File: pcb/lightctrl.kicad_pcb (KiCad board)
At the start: 2 copper layers, 76.8 x 36.8 mm, 30 parts, among them IC1 ESP-WROOM-02, P1 LED_CONN, P2 PROG, P3 IO, P4 BATT_SENSE, P5 5V, Q1 BSS138, Q2 IRF8788, SW1 SW_FLASH, SW2 SW_RST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

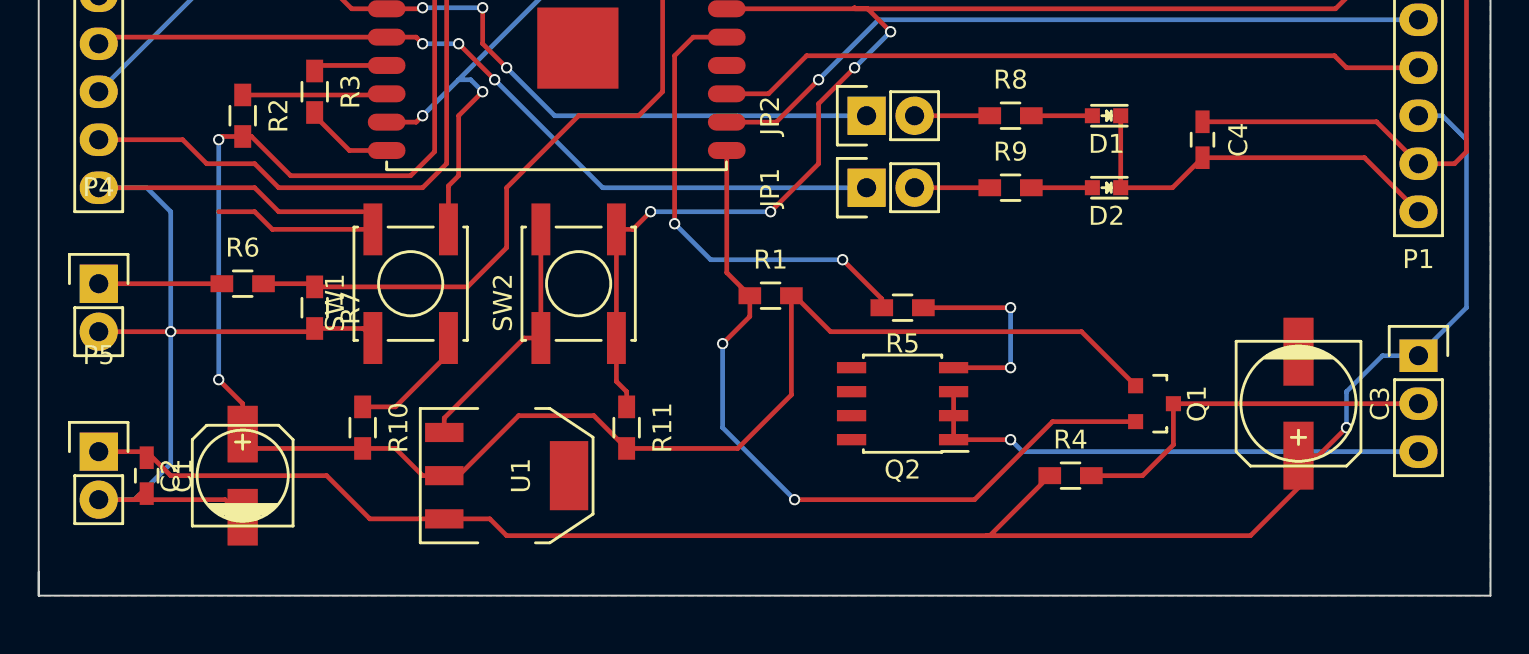
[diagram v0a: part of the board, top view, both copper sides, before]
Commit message: Thicker power traces
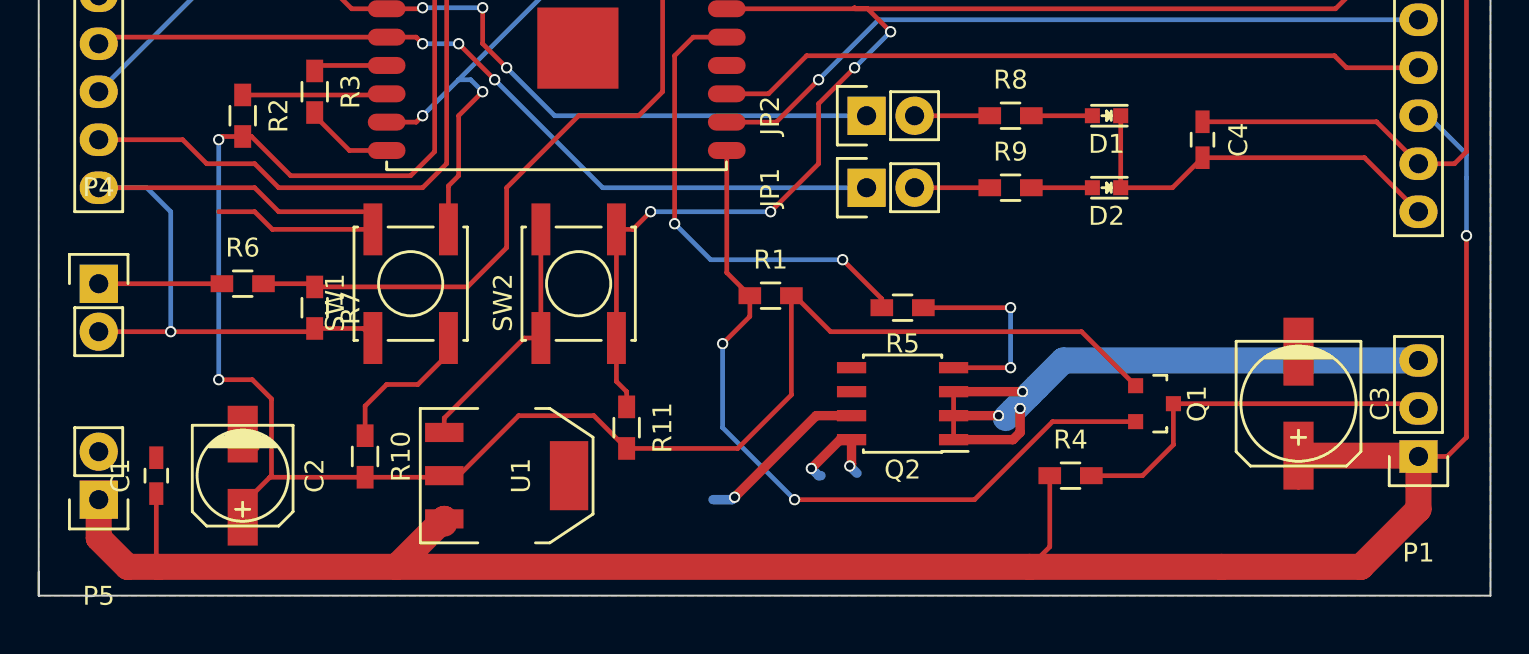
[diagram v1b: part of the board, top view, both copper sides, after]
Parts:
- moved P1 5.33 mm to (213.4, 84.1), turned to 180 degrees
- moved P5 2.54 mm to (143.5, 86.4), turned to 180 degrees
- moved R10 1.53 mm to (157.6, 84.1)
- moved C1 0.51 mm to (146.6, 85.1), turned to 90 degrees
- turned C2 to 270 degrees
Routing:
- net +5V: track 98.0 -> 119.1 mm
- net Net-(P1-Pad3): track 27.4 -> 39.4 mm, vias 1 -> 3
- net GND: track 108.7 -> 103.9 mm, vias 1 -> 4
- net +3V3: track 116.1 -> 120.5 mm
- net /ESP8266/BOOT_SEL: track 74.0 -> 75.4 mm

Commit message: New stick layout form
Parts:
- moved P2 106.2 mm to (107.3, 52.1), turned to 270 degrees
- moved IC1 81.2 mm to (78.7, 69.8), turned to 90 degrees
- moved SW2 72.9 mm to (97.8, 59.1), turned to 180 degrees
- moved R3 71.8 mm to (226.4, 71.6), turned to 0 degrees
- moved R2 71.1 mm to (222.0, 71.6), turned to 0 degrees
- moved R10 68.8 mm to (222.0, 59.8), turned to 0 degrees
- moved P1 58.9 mm to (156.2, 69.8), turned to 270 degrees
- moved SW1 54.4 mm to (108.0, 59.1), turned to 180 degrees
- moved C3 52.9 mm to (158.8, 59.7), turned to 180 degrees
- moved R11 48.7 mm to (217.5, 66.9), turned to 0 degrees
- moved R1 48.4 mm to (226.4, 65.7)
- moved R4 46.0 mm to (153.7, 64.8), turned to 270 degrees
- moved Q2 43.8 mm to (146.1, 63.5), turned to 0 degrees
- moved R7 42.9 mm to (116.8, 56.5), turned to 0 degrees
- moved JP1 40.6 mm to (146.1, 55.9)
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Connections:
- Q2 pad 1: Net-(P1-Pad3) -> GND
- Q2 pad 2: Net-(P1-Pad3) -> GND
- Q2 pad 3: Net-(P1-Pad3) -> GND
- Q2 pad 5: GND -> Net-(P1-Pad3)
- Q2 pad 6: GND -> Net-(P1-Pad3)
- Q2 pad 7: GND -> Net-(P1-Pad3)
- Q2 pad 8: GND -> Net-(P1-Pad3)
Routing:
- net /ESP8266/CTS: track 102.6 -> 0.00 mm, vias 4 -> 0
- net /ESP8266/BOOT_SEL: track 75.4 -> 0.00 mm, vias 2 -> 0
- net +5V: track 119.1 -> 44.2 mm
- net +3V3: track 120.5 -> 60.1 mm, vias 2 -> 0
- net GND: track 103.9 -> 55.4 mm, vias 4 -> 0
- net /ESP8266/IO16: track 45.4 -> 0.00 mm
- net /ESP8266/IO12: track 44.4 -> 0.00 mm, vias 3 -> 0
- net /ESP8266/IO13: track 44.1 -> 0.00 mm, vias 3 -> 0
- net /ESP8266/LED_DATA: track 40.9 -> 0.00 mm, vias 2 -> 0
- net /ESP8266/RXI: track 38.9 -> 0.00 mm, vias 1 -> 0
- net /ESP8266/TXO: track 37.7 -> 0.00 mm
- net /ESP8266/LED_PWR: track 25.1 -> 0.00 mm, vias 2 -> 0
- net Net-(P1-Pad3): track 39.4 -> 17.4 mm, vias 3 -> 0
- net /ESP8266/IO14: track 18.1 -> 0.00 mm, vias 1 -> 0
- net /ESP8266/WS2812_DATA: track 20.3 -> 3.98 mm
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- removed copper zone on B.Cu, net GND
- removed copper zone on F.Cu, net GND
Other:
- board size 76.8 x 36.8 mm -> 88.9 x 22.9 mm
- net class Default: clearance 0.2 -> 0.1524; trace_width 0.25 -> 0.1524; via_dia 0.6 -> 0.6858; via_drill 0.4 -> 0.3302
- rule trace_clearance: 0.2 -> 0.1524
- rule trace_min: 0.2 -> 0.1524
- rule via_min_drill: 0.3 -> 0.3302
- rule via_min_size: 0.4 -> 0.6858

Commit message: Pre-Compactifying checkpoint
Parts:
- moved R3 138.2 mm to (88.3, 74.3)
- moved R2 129.3 mm to (92.7, 74.3)
- moved R11 119.7 mm to (97.8, 67.3)
- moved R10 114.2 mm to (108.0, 65.4), turned to 270 degrees
- moved C4 113.2 mm to (97.8, 64.1)
- moved R1 86.7 mm to (140.3, 55.2)
- moved R5 81.0 mm to (141.0, 64.1), turned to 90 degrees
- moved Q1 71.9 mm to (140.3, 58.4), turned to 180 degrees
- moved P3 25.1 mm to (107.3, 69.8)
- moved P4 24.7 mm to (111.1, 36.8)
- moved C2 22.2 mm to (134.6, 55.9), turned to 270 degrees
- moved R6 11.5 mm to (115.6, 43.2)
- moved R7 11.5 mm to (115.6, 45.1)
- moved R4 0.90 mm to (154.3, 65.4)
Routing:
- net +3V3: track 60.1 -> 18.7 mm
- net Net-(IC1-Pad16): track 39.7 -> 1.91 mm
- net /ESP8266/WS2812_DATA: track 3.98 -> 23.5 mm, vias 0 -> 2
- net /ESP8266/LED_DATA: track 0.00 -> 2.24 mm
- net +5V: track 44.2 -> 43.3 mm

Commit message: Placement done
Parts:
- moved P4 30.5 mm to (111.8, 67.3), turned to 0 degrees
- moved R7 24.7 mm to (102.9, 66.3), turned to 180 degrees
- moved R6 24.6 mm to (107.2, 66.3)
- moved C1 17.8 mm to (124.5, 67.9)
- moved C2 17.8 mm to (116.8, 55.9)
- moved C3 17.8 mm to (141.0, 59.7)
- moved D1 17.8 mm to (146.1, 51.4)
- moved D2 17.8 mm to (146.1, 54.0)
- moved JP1 17.8 mm to (128.3, 55.9)
- moved JP2 17.8 mm to (128.3, 52.1)
- moved P1 17.8 mm to (138.4, 69.8)
- moved P5 17.8 mm to (146.1, 69.8)
- moved Q1 17.8 mm to (122.6, 58.4)
- moved Q2 17.8 mm to (128.3, 63.5)
- moved R1 17.8 mm to (122.6, 55.2)
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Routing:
- net +3V3: track 18.7 -> 79.7 mm
- net Net-(IC1-Pad6): track 0.00 -> 17.0 mm
- net /ESP8266/BOOT_SEL: track 0.00 -> 13.6 mm
- net /ESP8266/CTS: track 0.00 -> 13.2 mm
- net Net-(IC1-Pad7): track 0.00 -> 11.6 mm
- net GND: track 55.4 -> 66.9 mm
- net +BATT: track 0.17 -> 3.89 mm
- net Net-(Q2-Pad4): track 0.00 -> 2.45 mm
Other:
- board size 88.9 x 22.9 mm -> 71.1 x 22.9 mm

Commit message: Routing finished
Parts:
- moved R3 3.56 mm to (95.2, 66.3)
- moved R2 2.54 mm to (98.6, 66.3)
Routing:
- net /ESP8266/IO12: track 0.00 -> 62.3 mm, vias 0 -> 2
- net /ESP8266/IO13: track 0.00 -> 57.7 mm, vias 0 -> 6
- net /ESP8266/LED_PWR: track 0.00 -> 45.4 mm, vias 0 -> 4
- net +5V: track 43.3 -> 79.3 mm, vias 1 -> 3
- net /ESP8266/LED_DATA: track 2.24 -> 36.8 mm, vias 0 -> 2
- net Net-(IC1-Pad16): track 2.12 -> 31.7 mm, vias 0 -> 2
- net /ESP8266/BOOT_SEL: track 13.6 -> 42.9 mm, vias 0 -> 4
- net /ESP8266/IO16: track 0.00 -> 29.1 mm, vias 0 -> 2
- net /ESP8266/IO14: track 0.00 -> 28.8 mm
- net +3V3: track 79.7 -> 102.4 mm
- net /ESP8266/CTS: track 13.2 -> 34.5 mm
- net /ESP8266/RXI: track 0.00 -> 20.2 mm, vias 0 -> 2
- net /ESP8266/TXO: track 0.00 -> 18.0 mm, vias 0 -> 2
- net GND: track 66.9 -> 78.9 mm, vias 0 -> 3
- net Net-(IC1-Pad6): track 17.0 -> 12.8 mm
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- added copper zone on B.Cu, net GND
- added copper zone on F.Cu, net GND

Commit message: Silkscreen finished
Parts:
- renumbered P5 to 5V, P4 to BATT_SENS, SW1 to FLASH, P1 to LED, P2 to PROG, SW2 to RST
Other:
- board text added: "<<</>>"
- board text added: "IO"
- board text added: "Wi-Fi LED Controller jan@legxaro.de chris@priseko.de"
- board text added: "https://github.com/polygon/lightctrl"
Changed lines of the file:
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@@
     (area 71.511399 48.4576 228.602403 82.8424)
     (thickness 1.6002)
-    (drawings 5)
+    (drawings 9)
     (tracks 349)
     (zones 0)
@@
     (descr "Module, ESP-8266, ESP-13-WROOM-02, 18 pad, SMD")
     (tags "Module ESP-8266 ESP8266")
-    (fp_text reference IC1 (at -3 -5 90) (layer F.SilkS)
+    (fp_text reference IC1 (at 4.318 13.97 270) (layer F.SilkS)
       (effects (font (size 1 1) (thickness 0.15)))
     )
@@
     (tags "capacitor 0603")
     (attr smd)
-    (fp_text reference C1 (at 0 -1.9) (layer F.SilkS)
+    (fp_text reference C1 (at 1.016 1.397) (layer F.SilkS)
       (effects (font (size 1 1) (thickness 0.15)))
     )
@@
     (descr "SMT capacitor, aluminium electrolytic, 5x5.3")
     (attr smd)
-    (fp_text reference C2 (at 0 -3.81 270) (layer F.SilkS)
+    (fp_text reference C2 (at -3.556 -2.032 360) (layer F.SilkS)
       (effects (font (size 1 1) (thickness 0.15)))
     )
@@
     (descr "SMT capacitor, aluminium electrolytic, 6.3x7.7")
     (attr smd)
-    (fp_text reference C3 (at 0 -4.318 180) (layer F.SilkS)
+    (fp_text reference C3 (at -4.318 -2.794 180) (layer F.SilkS)
       (effects (font (size 1 1) (thickness 0.15)))
     )
@@
     (tags "capacitor 0603")
     (attr smd)
-    (fp_text reference C4 (at 0 -1.9 180) (layer F.SilkS)
+    (fp_text reference C4 (at -0.762 1.397 180) (layer F.SilkS)
       (effects (font (size 1 1) (thickness 0.15)))
     )
@@
     (tags "LED led 0603 SMD smd SMT smt smdled SMDLED smtled SMTLED")
     (attr smd)
-    (fp_text reference D1 (at 0 -1.5 180) (layer F.SilkS)
-      (effects (font (size 1 1) (thickness 0.15)))
+    (fp_text reference D1 (at 2.032 -0.127 180) (layer F.SilkS)
+      (effects (font (size 0.762 0.762) (thickness 0.15)))
     )
     (fp_text value LED (at 0 1.5 180) (layer F.Fab)
@@
     (tags "LED led 0603 SMD smd SMT smt smdled SMDLED smtled SMTLED")
     (attr smd)
-    (fp_text reference D2 (at 0 -1.5 180) (layer F.SilkS)
-      (effects (font (size 1 1) (thickness 0.15)))
+    (fp_text reference D2 (at 2.032 -0.127 180) (layer F.SilkS)
+      (effects (font (size 0.762 0.762) (thickness 0.15)))
     )
     (fp_text value LED (at 0 1.5 180) (layer F.Fab)
@@
     (descr "Through hole pin header")
     (tags "pin header")
-    (fp_text reference JP1 (at 0 -5.1 90) (layer F.SilkS)
+    (fp_text reference JP1 (at 0 5.334 180) (layer F.SilkS)
       (effects (font (size 1 1) (thickness 0.15)))
     )
@@
     (descr "Through hole pin header")
     (tags "pin header")
-    (fp_text reference JP2 (at 0 -5.1 90) (layer F.SilkS)
+    (fp_text reference JP2 (at 0 5.334 180) (layer F.SilkS)
       (effects (font (size 1 1) (thickness 0.15)))
     )
@@
     (descr "Through hole pin header")
     (tags "pin header")
-    (fp_text reference P1 (at 0 -5.1 270) (layer F.SilkS)
+    (fp_text reference LED (at 0 -3.048 360) (layer F.SilkS)
       (effects (font (size 1 1) (thickness 0.15)))
     )
@@
     (descr "Through hole pin header")
     (tags "pin header")
-    (fp_text reference P2 (at 0 -5.1 270) (layer F.SilkS)
+    (fp_text reference PROG (at 2.54 0.127 360) (layer F.SilkS)
       (effects (font (size 1 1) (thickness 0.15)))
     )
@@
     (descr "Through hole pin header")
     (tags "pin header")
-    (fp_text reference P4 (at 0 -5.1) (layer F.SilkS)
-      (effects (font (size 1 1) (thickness 0.15)))
+    (fp_text reference BATT_SENS (at -0.508 -2.286) (layer F.SilkS)
+      (effects (font (size 0.762 0.762) (thickness 0.15)))
     )
     (fp_text value BATT_SENSE (at 0 -3.1) (layer F.Fab)
@@
     (descr "Through hole pin header")
     (tags "pin header")
-    (fp_text reference P5 (at 0 -5.1 180) (layer F.SilkS)
+    (fp_text reference 5V (at 0 4.572 180) (layer F.SilkS)
       (effects (font (size 1 1) (thickness 0.15)))
     )
@@
     (tags SOT-23)
     (attr smd)
-    (fp_text reference Q1 (at 0 -2.25 180) (layer F.SilkS)
+    (fp_text reference Q1 (at -2.667 -0.254 270) (layer F.SilkS)
       (effects (font (size 1 1) (thickness 0.15)))
     )
@@
     (tags "resistor 0603")
     (attr smd)
-    (fp_text reference R1 (at 0 -1.9) (layer F.SilkS)
+    (fp_text reference R1 (at 0.127 -1.651) (layer F.SilkS)
       (effects (font (size 1 1) (thickness 0.15)))
     )
@@
     (tags "resistor 0603")
     (attr smd)
-    (fp_text reference R2 (at 0 -1.9 270) (layer F.SilkS)
+    (fp_text reference R2 (at -1.27 -1.524 360) (layer F.SilkS)
       (effects (font (size 1 1) (thickness 0.15)))
     )
@@
     (tags "resistor 0603")
     (attr smd)
-    (fp_text reference R3 (at 0 -1.9 270) (layer F.SilkS)
+    (fp_text reference R3 (at -1.27 -1.524 360) (layer F.SilkS)
       (effects (font (size 1 1) (thickness 0.15)))
     )
@@
     (tags "resistor 0603")
     (attr smd)
-    (fp_text reference R4 (at 0 -1.9 270) (layer F.SilkS)
+    (fp_text reference R4 (at 0.127 -1.905 360) (layer F.SilkS)
       (effects (font (size 1 1) (thickness 0.15)))
     )
@@
     (tags "resistor 0603")
     (attr smd)
-    (fp_text reference R5 (at 0 -1.9 90) (layer F.SilkS)
+    (fp_text reference R5 (at 2.667 -0.254 180) (layer F.SilkS)
       (effects (font (size 1 1) (thickness 0.15)))
     )
@@
     (tags "resistor 0603")
     (attr smd)
-    (fp_text reference R6 (at 0 -1.9 180) (layer F.SilkS)
+    (fp_text reference R6 (at 1.016 1.524 180) (layer F.SilkS)
       (effects (font (size 1 1) (thickness 0.15)))
     )
@@
     (tags "resistor 0603")
     (attr smd)
-    (fp_text reference R7 (at 0 -1.9 180) (layer F.SilkS)
+    (fp_text reference R7 (at 0 1.524 180) (layer F.SilkS)
       (effects (font (size 1 1) (thickness 0.15)))
     )
@@
     (tags "resistor 0603")
     (attr smd)
-    (fp_text reference R8 (at 0 -1.9) (layer F.SilkS)
+    (fp_text reference R8 (at -2.794 0.127) (layer F.SilkS)
       (effects (font (size 1 1) (thickness 0.15)))
     )
@@
     (tags "resistor 0603")
     (attr smd)
-    (fp_text reference R9 (at 0 -1.9) (layer F.SilkS)
+    (fp_text reference R9 (at -2.794 0.127) (layer F.SilkS)
       (effects (font (size 1 1) (thickness 0.15)))
     )
@@
     (tags "resistor 0603")
     (attr smd)
-    (fp_text reference R10 (at 0 -1.9) (layer F.SilkS)
+    (fp_text reference R10 (at 0 -1.524) (layer F.SilkS)
       (effects (font (size 1 1) (thickness 0.15)))
     )
@@
     (tags "resistor 0603")
     (attr smd)
-    (fp_text reference R11 (at 0 -1.9) (layer F.SilkS)
+    (fp_text reference R11 (at 0.508 -1.397) (layer F.SilkS)
       (effects (font (size 1 1) (thickness 0.15)))
     )
@@
     (descr "Light Touch Switch")
     (attr smd)
-    (fp_text reference SW1 (at -1 -4 180) (layer F.SilkS)
+    (fp_text reference FLASH (at -1.016 3.81 180) (layer F.SilkS)
       (effects (font (size 1 1) (thickness 0.15)))
     )
@@
     (descr "Light Touch Switch")
     (attr smd)
-    (fp_text reference SW2 (at -1 -4 180) (layer F.SilkS)
+    (fp_text reference RST (at -1.778 3.81 180) (layer F.SilkS)
       (effects (font (size 1 1) (thickness 0.15)))
     )
@@
     (tags "CMS SOT")
     (attr smd)
-    (fp_text reference U1 (at 0 -0.762) (layer F.SilkS)
+    (fp_text reference U1 (at 4.572 4.064) (layer F.SilkS)
       (effects (font (size 1 1) (thickness 0.15)))
     )
@@
     (tags "SOIC 1.27")
     (attr smd)
-    (fp_text reference Q2 (at 0 -3.5) (layer F.SilkS)
+    (fp_text reference Q2 (at 1.27 3.556) (layer F.SilkS)
       (effects (font (size 1 1) (thickness 0.15)))
     )
@@
     )
   )
+  (gr_text https://github.com/polygon/lightctrl (at 78.1685 70.2945) (layer B.SilkS)
+    (effects (font (size 1.5 1.5) (thickness 0.3)) (justify right mirror))
+  )
+  (gr_text "Wi-Fi LED Controller\njan@legxaro.de\nchris@priseko.de" (at 147.32 67.945) (layer B.SilkS)
+    (effects (font (size 1.5 1.5) (thickness 0.3)) (justify left mirror))
+  )
+  (gr_text <<</>> (at 122.809 55.626) (layer B.SilkS)
+    (effects (font (size 7 7) (thickness 1.75)) (justify mirror))
+  )
+  (gr_text IO (at 108.458 67.818) (layer F.SilkS)
+    (effects (font (size 0.762 0.762) (thickness 0.1905)))
+  )
   (gr_line (start 148.59 49.53) (end 142.24 49.53) (angle 90) (layer Edge.Cuts) (width 0.1))

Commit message: Fixing part names in PCB
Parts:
- renumbered LED to P1, PROG to P2, BATT_SENS to P4, 5V to P5, FLASH to SW1, RST to SW2
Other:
- board text added: "5V"
- board text added: "BATT_SENS"
- board text added: "FLASH"
- board text added: "LED"
- board text added: "PROG"
- board text added: "RST"
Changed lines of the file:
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@@
     (links 73)
     (no_connects 0)
-    (area 71.511399 48.4576 228.602403 82.8424)
+    (area 71.511399 48.101 149.017334 73.886924)
     (thickness 1.6002)
-    (drawings 9)
+    (drawings 15)
     (tracks 349)
     (zones 0)
@@
   (page A4)
   (layers
-    (0 F.Cu signal)
-    (31 B.Cu signal)
+    (0 F.Cu signal hide)
+    (31 B.Cu signal hide)
     (36 B.SilkS user)
     (37 F.SilkS user)
@@
   )
   (setup
-    (last_trace_width 0.5)
+    (last_trace_width 0.1524)
     (user_trace_width 0.25)
     (user_trace_width 0.5)
@@
     (descr "Through hole pin header")
     (tags "pin header")
-    (fp_text reference LED (at 0 -3.048 360) (layer F.SilkS)
+    (fp_text reference P1 (at 0 -3.048 360) (layer F.SilkS) hide
       (effects (font (size 1 1) (thickness 0.15)))
     )
@@
     (descr "Through hole pin header")
     (tags "pin header")
-    (fp_text reference PROG (at 2.54 0.127 360) (layer F.SilkS)
-      (effects (font (size 1 1) (thickness 0.15)))
-    )
-    (fp_text value PROG (at 0 -3.1 270) (layer F.Fab)
+    (fp_text reference P2 (at 2.3749 -0.7747 360) (layer F.SilkS) hide
+      (effects (font (size 1 1) (thickness 0.15)))
+    )
+    (fp_text value PROG (at 0 -3.1 360) (layer F.SilkS) hide
       (effects (font (size 1 1) (thickness 0.15)))
     )
@@
     (descr "Through hole pin header")
     (tags "pin header")
-    (fp_text reference BATT_SENS (at -0.508 -2.286) (layer F.SilkS)
+    (fp_text reference P4 (at -0.508 -2.286) (layer F.SilkS) hide
       (effects (font (size 0.762 0.762) (thickness 0.15)))
     )
@@
     (descr "Through hole pin header")
     (tags "pin header")
-    (fp_text reference 5V (at 0 4.572 180) (layer F.SilkS)
+    (fp_text reference P5 (at 0 4.572 180) (layer F.SilkS) hide
       (effects (font (size 1 1) (thickness 0.15)))
     )
@@
     (descr "Light Touch Switch")
     (attr smd)
-    (fp_text reference FLASH (at -1.016 3.81 180) (layer F.SilkS)
+    (fp_text reference SW1 (at -1.016 3.81 180) (layer F.SilkS) hide
       (effects (font (size 1 1) (thickness 0.15)))
     )
@@
     (descr "Light Touch Switch")
     (attr smd)
-    (fp_text reference RST (at -1.778 3.81 180) (layer F.SilkS)
+    (fp_text reference SW2 (at -1.778 3.81 180) (layer F.SilkS) hide
       (effects (font (size 1 1) (thickness 0.15)))
     )
@@
     )
   )
+  (gr_text FLASH (at 108.966 57.15) (layer F.SilkS)
+    (effects (font (size 1 1) (thickness 0.15)))
+  )
+  (gr_text RST (at 99.568 57.15) (layer F.SilkS)
+    (effects (font (size 1 1) (thickness 0.15)))
+  )
+  (gr_text LED (at 141.478 69.85) (layer F.SilkS)
+    (effects (font (size 1 1) (thickness 0.15)))
+  )
+  (gr_text 5V (at 146.05 65.278) (layer F.SilkS)
+    (effects (font (size 1 1) (thickness 0.15)))
+  )
+  (gr_text BATT_SENS (at 111.76 65.024) (layer F.SilkS)
+    (effects (font (size 0.5 0.5) (thickness 0.1)))
+  )
+  (gr_text PROG (at 107.188 54.61) (layer F.SilkS)
+    (effects (font (size 1 1) (thickness 0.15)))
+  )
   (gr_text https://github.com/polygon/lightctrl (at 78.1685 70.2945) (layer B.SilkS)
     (effects (font (size 1.5 1.5) (thickness 0.3)) (justify right mirror))
@@
     (effects (font (size 7 7) (thickness 1.75)) (justify mirror))
   )
-  (gr_text IO (at 108.458 67.818) (layer F.SilkS)
-    (effects (font (size 0.762 0.762) (thickness 0.1905)))
+  (gr_text IO (at 108.458 67.564) (layer F.SilkS)
+    (effects (font (size 1 1) (thickness 0.15)))
   )
   (gr_line (start 148.59 49.53) (end 142.24 49.53) (angle 90) (layer Edge.Cuts) (width 0.1))
